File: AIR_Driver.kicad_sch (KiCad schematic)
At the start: 5 parts, among them J7 Conn_01x04, Q3 DMN61D8LQ, Q4 DMN61D8LQ

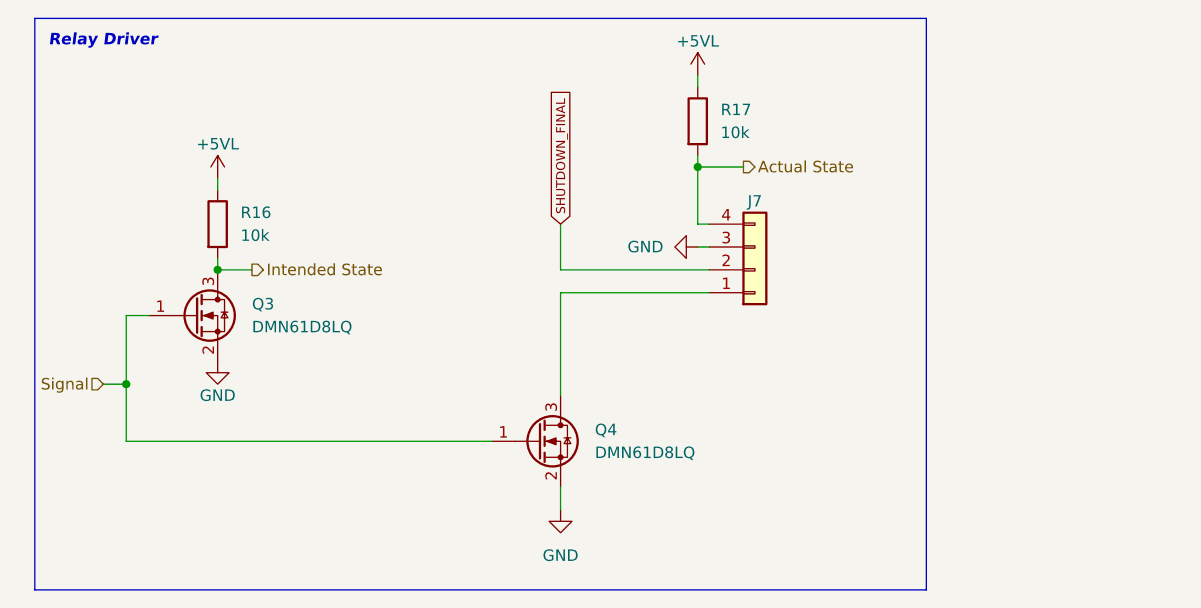
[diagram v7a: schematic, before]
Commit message: *: Switch to new AIR driving MOSFETs
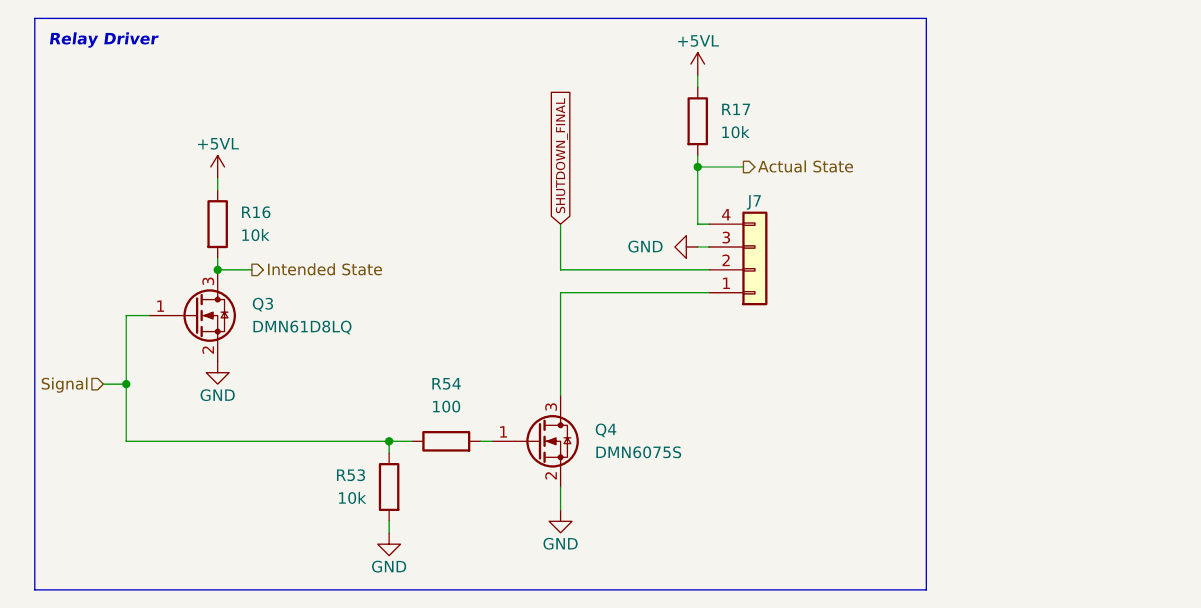
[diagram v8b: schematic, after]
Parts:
- removed Q4: DMN61D8LQ, Package_TO_SOT_SMD:SOT-23, symbol Transistor_FET:DMN61D8LQ
- added Q4: DMN6075S, Package_TO_SOT_SMD:SOT-23, symbol Transistor_FET:DMN6075S
- added R53: 10k, Resistor_SMD:R_0603_1608Metric, symbol Device:R
- added R54: 100, Resistor_SMD:R_0603_1608Metric, symbol Device:R
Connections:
- net GND: now also Q4.2 (S), R53.2
- net Signal: now also R53.1, R54.1
- net at J7.1 (Pin_1): now also Q4.3 (D)
- new net: Q4.1 (G), R54.2
